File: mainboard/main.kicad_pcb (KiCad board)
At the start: 2 copper layers, 13 parts, among them U1 LevelShifter

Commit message: merge boards
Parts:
- removed Con_MainBoard2PowerBoard1: Conn_01x09_Female, Connector_PinSocket_2.54mm:PinSocket_1x11_P2.54mm_Vertical
- added Battery_Connector1: Conn_01x06, Connector_JST:JST_XH_B6B-XH-A_1x06_P2.50mm_Vertical, F.Cu at (147.3, 101.6)
- added C1: 1uF, Capacitor_THT:CP_Radial_D5.0mm_P2.50mm, F.Cu at (175.3, 101.6)
- added C2: 1uF, Capacitor_THT:CP_Radial_D5.0mm_P2.50mm, F.Cu at (157.5, 101.6)
- added CellVoltageOpAmp1: LM358, Package_DIP:DIP-8_W7.62mm_Socket, F.Cu at (172.7, 88.9)
- added Con_Stepdown_Board1: Conn_01x03, Connector_JST:JST_XH_B3B-XH-A_1x03_P2.50mm_Vertical, F.Cu at (188.0, 81.3)
- added CurrentDrawOpAmp1: LM358, Package_DIP:DIP-8_W7.62mm_Socket, F.Cu at (154.9, 88.9)
- added CurrentSensor1: ACS712Breakout, CustomFootprints:ACS712BreakoutBoardUpSideDown, F.Cu at (124.5, 88.9)
- added Diode1: D, Diode_THT:D_T-1_P5.08mm_Horizontal, F.Cu at (147.3, 73.7)
- added Q1: TIP120, Package_TO_SOT_THT:TO-220-3_Vertical, F.Cu at (115.6, 80.0)
- added RV1: R_POT_TRIM, Potentiometer_THT:Potentiometer_Bourns_3296W_Vertical, F.Cu at (127.0, 78.7)
- added R_Cell1_Vdiv_A1: 33K, Resistor_THT:R_Axial_DIN0207_L6.3mm_D2.5mm_P7.62mm_Horizontal, F.Cu at (170.2, 83.8)
- added R_Cell1_Vdiv_B1: 100K, Resistor_THT:R_Axial_DIN0207_L6.3mm_D2.5mm_P2.54mm_Vertical, F.Cu at (177.8, 83.8)
- added R_I_1: 10K, Resistor_THT:R_Axial_DIN0207_L6.3mm_D2.5mm_P5.08mm_Vertical, F.Cu at (142.2, 88.9)
- added R_I_2: 33K, Resistor_THT:R_Axial_DIN0207_L6.3mm_D2.5mm_P5.08mm_Vertical, F.Cu at (147.3, 91.4)
- added R_I_3: 33K, Resistor_THT:R_Axial_DIN0207_L6.3mm_D2.5mm_P2.54mm_Vertical, F.Cu at (144.8, 83.8)
- added R_I_4: 22K, Resistor_THT:R_Axial_DIN0207_L6.3mm_D2.5mm_P2.54mm_Vertical, F.Cu at (147.3, 91.4)
- added R_T1: 1K, Resistor_THT:R_Axial_DIN0207_L6.3mm_D2.5mm_P5.08mm_Vertical, F.Cu at (124.5, 100.3)
- added R_V_Cell2_1: 47K, Resistor_THT:R_Axial_DIN0207_L6.3mm_D2.5mm_P2.54mm_Vertical, F.Cu at (167.6, 91.4)
- added R_V_Cell2_2: 47K, Resistor_THT:R_Axial_DIN0207_L6.3mm_D2.5mm_P2.54mm_Vertical, F.Cu at (165.1, 101.6)
- added R_V_Cell2_3: 33K, Resistor_THT:R_Axial_DIN0207_L6.3mm_D2.5mm_P2.54mm_Vertical, F.Cu at (167.6, 91.4)
- added R_V_Cell2_4: 33K, Resistor_THT:R_Axial_DIN0207_L6.3mm_D2.5mm_P2.54mm_Vertical, F.Cu at (167.6, 99.1)
- added R_V_Cell3_1: 47K, Resistor_THT:R_Axial_DIN0207_L6.3mm_D2.5mm_P5.08mm_Vertical, F.Cu at (185.4, 94.0)
- added R_V_Cell3_2: 47K, Resistor_THT:R_Axial_DIN0207_L6.3mm_D2.5mm_P2.54mm_Vertical, F.Cu at (188.0, 96.5)
- added R_V_Cell3_3: 33K, Resistor_THT:R_Axial_DIN0207_L6.3mm_D2.5mm_P2.54mm_Vertical, F.Cu at (185.4, 94.0)
- added R_V_Cell3_4: 33K, Resistor_THT:R_Axial_DIN0207_L6.3mm_D2.5mm_P2.54mm_Vertical, F.Cu at (188.0, 91.4)
- added Switch_Connector1: Conn_01x04, Connector_JST:JST_XH_B2B-XH-A_1x02_P2.50mm_Vertical, F.Cu at (141.0, 78.7)
- moved AdOn_Connector1 18.2 mm to (116.8, 45.7)
- moved Con_Switch1 8.03 mm to (175.3, 76.2)
- moved U1 7.62 mm to (129.5, 40.6)
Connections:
- MicroController1 pad 17: PowerIN -> P_IN
- MicroController1 pad 18: PCheck -> P_Check
- MicroController1 pad 19: Net-(Con_MainBoard2PowerBoard1-Pad6) -> op1
- MicroController1 pad 20: Net-(Con_MainBoard2PowerBoard1-Pad5) -> op2
- MicroController1 pad 21: Net-(Con_MainBoard2PowerBoard1-Pad4) -> op3
- MicroController1 pad 23: Net-(Con_MainBoard2PowerBoard1-Pad3) -> op4
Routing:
- net GND: track 193.1 -> 348.3 mm, vias 0 -> 1
- net +BATT: track 111.8 -> 248.0 mm
- net +5V: track 65.4 -> 196.2 mm, vias 0 -> 1
- net op1: track 0.00 -> 44.6 mm
- net Net-(Diode1-Pad1): track 0.00 -> 43.6 mm
- net BATT_Cell_2_3: track 0.00 -> 40.2 mm
- net BATT_Cell_1_2: track 0.00 -> 38.2 mm
- net P_Check: track 0.00 -> 35.7 mm
- net op3: track 0.00 -> 34.3 mm
- net op2: track 0.00 -> 30.7 mm
- net Net-(Battery_Connector1-Pad5): track 0.00 -> 28.7 mm
- net +3V3: track 166.3 -> 194.8 mm
- net I2C_SDA: track 70.2 -> 95.6 mm
- net Net-(CurrentSensor1-Pad5): track 0.00 -> 23.7 mm
- net PCheck: track 22.0 -> 0.00 mm
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
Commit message: first prototype
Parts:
- removed C1: 1uF, Capacitor_THT:CP_Radial_D5.0mm_P2.50mm
- removed CellVoltageOpAmp1: LM358, Package_DIP:DIP-8_W7.62mm_Socket
- removed R_Cell1_Vdiv_A1: 33K, Resistor_THT:R_Axial_DIN0207_L6.3mm_D2.5mm_P7.62mm_Horizontal
- removed R_Cell1_Vdiv_B1: 100K, Resistor_THT:R_Axial_DIN0207_L6.3mm_D2.5mm_P2.54mm_Vertical
- removed R_V_Cell2_1, R_V_Cell2_2, R_V_Cell3_2: 47K, Resistor_THT:R_Axial_DIN0207_L6.3mm_D2.5mm_P2.54mm_Vertical
- removed R_V_Cell2_3, R_V_Cell2_4, R_V_Cell3_3, R_V_Cell3_4: 33K, Resistor_THT:R_Axial_DIN0207_L6.3mm_D2.5mm_P2.54mm_Vertical
- removed R_V_Cell3_1: 47K, Resistor_THT:R_Axial_DIN0207_L6.3mm_D2.5mm_P5.08mm_Vertical
- added Diode2: D, Diode_THT:D_T-1_P5.08mm_Horizontal, F.Cu at (167.6, 94.0)
- added Diode3: D, Diode_THT:D_T-1_P5.08mm_Horizontal, F.Cu at (180.3, 96.5)
- added R1: ?, Resistor_THT:R_Axial_DIN0207_L6.3mm_D2.5mm_P2.54mm_Vertical, F.Cu at (146.1, 73.7)
- added REF**: MountingHole_2.2mm_M2, MountingHole:MountingHole_2.2mm_M2, F.Cu at (111.8, 102.9)
- added REF**: MountingHole_2.2mm_M2, MountingHole:MountingHole_2.2mm_M2, F.Cu at (190.5, 102.9)
- added REF**: MountingHole_2.2mm_M2, MountingHole:MountingHole_2.2mm_M2, F.Cu at (190.5, 29.2)
- added REF**: MountingHole_2.2mm_M2, MountingHole:MountingHole_2.2mm_M2, F.Cu at (111.8, 29.2)
- added RV2: R_POT3Bat, Potentiometer_THT:Potentiometer_Bourns_3296W_Vertical, F.Cu at (167.6, 85.1)
- added RV3: R_POT2, Potentiometer_THT:Potentiometer_Bourns_3296W_Vertical, F.Cu at (174.0, 85.1)
- added RV4: R_POT1, Potentiometer_THT:Potentiometer_Bourns_3296W_Vertical, F.Cu at (180.3, 85.1)
- MicroController1: footprint CustomFootprints:Arduino_Pro_Mini_Socket_IZOKEE -> CustomFootprints:Arduino_Pro_Mini_Socket_IZOKEE_no_programming
- moved R_T1 25.4 mm to (123.2, 74.9)
- moved Diode1sw1 1.27 mm to (148.6, 73.7)
- renumbered Diode1 to Diode1sw1
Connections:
- Con_Switch1 pad 3: +3V3 -> GND
- Diode1sw1 pad 1: Net-(Diode1-Pad1) -> Net-(Diode1sw1-Pad1)
- RV1 pad 3: Net-(Diode1-Pad1) -> Net-(Diode1sw1-Pad1)
- R_T1 pad 1: Net-(Diode1-Pad1) -> Net-(Diode1sw1-Pad1)
- Switch_Connector1 pad 2: Net-(Diode1-Pad1) -> Net-(R1-Pad1)
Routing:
- net Net-(Diode1-Pad1): track 43.6 -> 0.00 mm
- net Net-(Diode1sw1-Pad1): track 0.00 -> 31.9 mm
- net BATT_Cell_2_3: track 40.2 -> 21.4 mm
- net GND: track 348.3 -> 329.5 mm, vias 1 -> 0
- net +5V: track 196.2 -> 179.2 mm, vias 1 -> 0
- net Net-(Q1-Pad1): track 21.9 -> 6.13 mm
- net +BATT: track 248.0 -> 262.5 mm
- net op3: track 34.3 -> 22.7 mm
- net Net-(R1-Pad1): track 0.00 -> 10.4 mm
- net Net-(CellVoltageOpAmp1-Pad3): track 9.72 -> 0.00 mm
- net +3V3: track 194.8 -> 186.0 mm
- net Net-(CellVoltageOpAmp1-Pad5): track 8.67 -> 0.00 mm
- net op2: track 30.7 -> 23.3 mm
- net Net-(Diode3-Pad1): track 0.00 -> 6.35 mm
- net op4: track 19.4 -> 25.1 mm
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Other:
- board text added: "CV & RS"

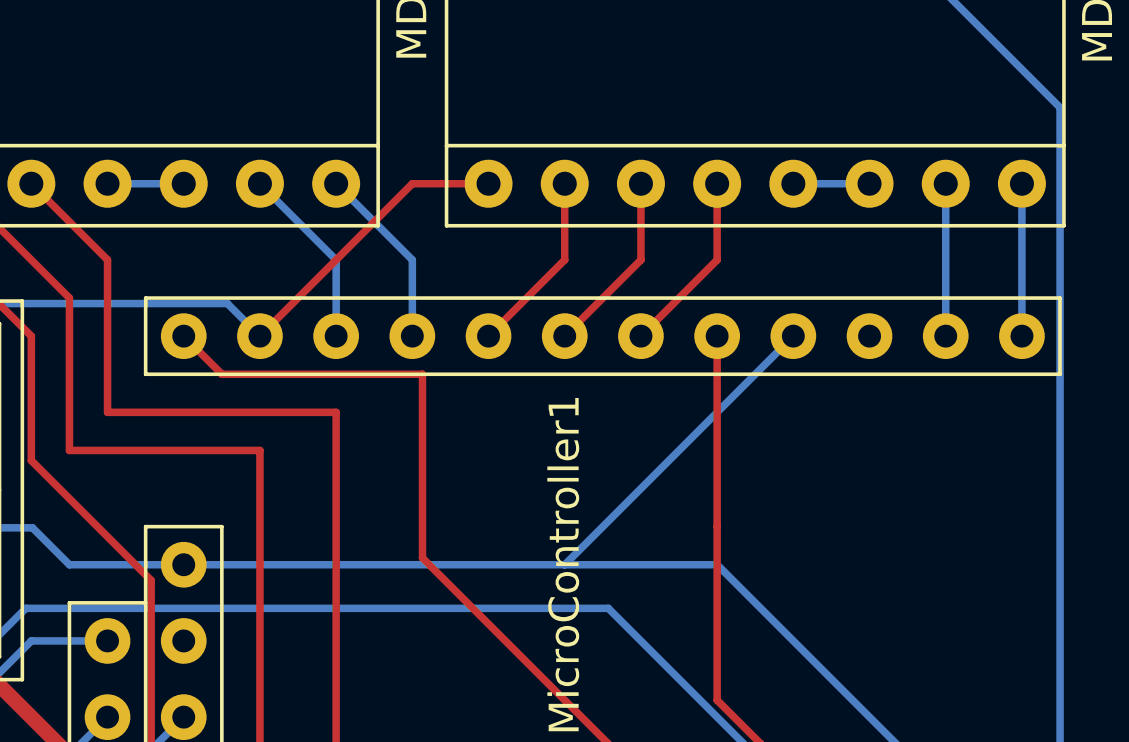
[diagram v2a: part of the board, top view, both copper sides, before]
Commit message: pwm pins
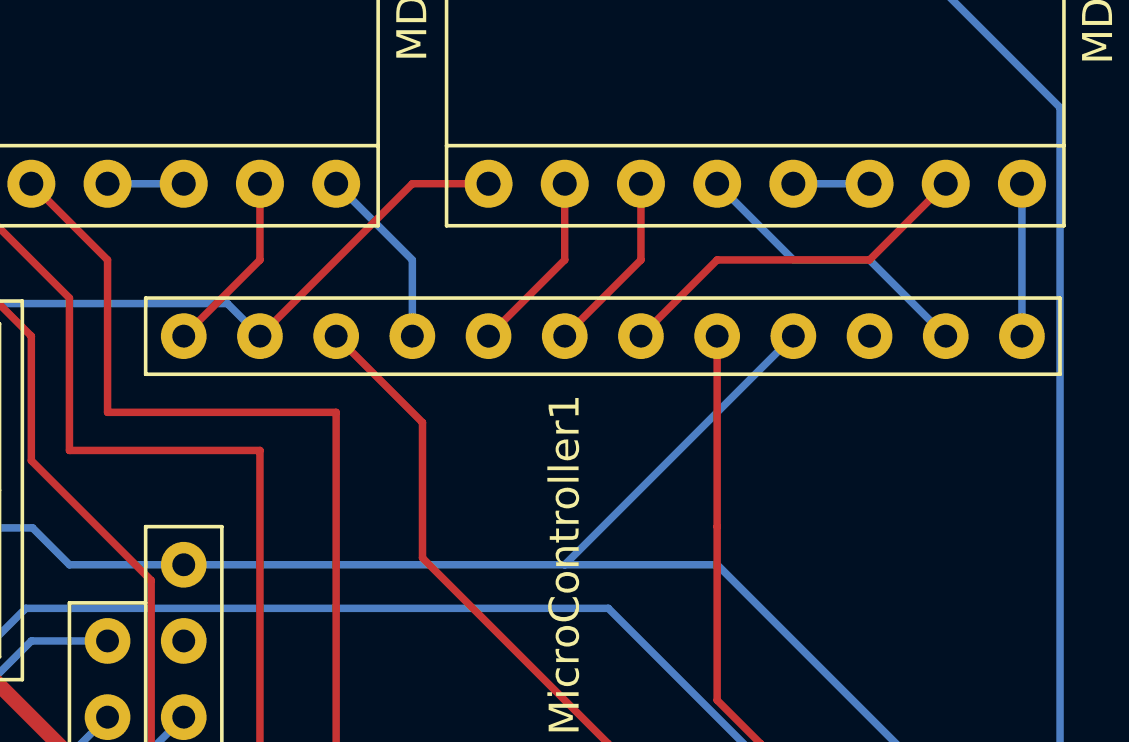
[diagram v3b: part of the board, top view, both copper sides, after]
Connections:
- MicroController1 pad 10: Step_L -> Sw2
- MicroController1 pad 12: Sw2 -> Step_L
- MicroController1 pad 2: Step_R -> MS3_R
- MicroController1 pad 6: MS3_R -> Step_R
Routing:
- net Step_R: track 5.08 -> 12.3 mm
- net Sw2: track 33.1 -> 27.1 mm
- net MS3_R: track 6.13 -> 9.72 mm
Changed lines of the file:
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@@
     (thickness 1.6)
     (drawings 22)
-    (tracks 337)
+    (tracks 339)
     (zones 0)
     (modules 36)
@@
   )
   (setup
-    (last_trace_width 0.5)
+    (last_trace_width 0.25)
     (user_trace_width 0.25)
     (user_trace_width 0.5)
@@
       (net 9 Dir_R))
     (pad 2 thru_hole circle (at -7.62 -10.16 270) (size 1.524 1.524) (drill 0.762) (layers *.Cu *.Mask)
-      (net 10 Step_R))
+      (net 35 MS3_R))
     (pad 3 thru_hole circle (at -7.62 -7.62 270) (size 1.524 1.524) (drill 0.762) (layers *.Cu *.Mask)
       (net 25 "Net-(MicroController1-Pad3)"))
@@
       (net 41 Sw1))
     (pad 6 thru_hole circle (at -7.62 0 270) (size 1.524 1.524) (drill 0.762) (layers *.Cu *.Mask)
-      (net 35 MS3_R))
+      (net 10 Step_R))
     (pad 7 thru_hole circle (at -7.62 2.54 270) (size 1.524 1.524) (drill 0.762) (layers *.Cu *.Mask)
       (net 36 MS2_R))
@@
       (net 6 Dir_L))
     (pad 10 thru_hole circle (at -7.62 10.16 270) (size 1.524 1.524) (drill 0.762) (layers *.Cu *.Mask)
-      (net 7 Step_L))
+      (net 42 Sw2))
     (pad 11 thru_hole circle (at -7.62 12.7 270) (size 1.524 1.524) (drill 0.762) (layers *.Cu *.Mask)
       (net 8 Enable_Steppers))
     (pad 12 thru_hole circle (at -7.62 15.24 270) (size 1.524 1.524) (drill 0.762) (layers *.Cu *.Mask)
-      (net 42 Sw2))
+      (net 7 Step_L))
     (pad 13 thru_hole circle (at 7.62 15.24 270) (size 1.524 1.524) (drill 0.762) (layers *.Cu *.Mask)
       (net 34 MS1_L))
@@
   (segment (start 167.64 53.34) (end 167.64 50.8) (width 0.25) (layer B.Cu) (net 6))
   (segment (start 167.64 50.8) (end 165.1 48.26) (width 0.25) (layer B.Cu) (net 6))
-  (segment (start 165.1 50.8) (end 162.56 48.26) (width 0.25) (layer B.Cu) (net 7))
-  (segment (start 165.1 53.34) (end 165.1 50.8) (width 0.25) (layer B.Cu) (net 7))
+  (segment (start 162.56 50.8) (end 160.02 53.34) (width 0.25) (layer F.Cu) (net 7))
+  (segment (start 162.56 48.26) (end 162.56 50.8) (width 0.25) (layer F.Cu) (net 7))
   (segment (start 151.312999 52.252999) (end 148.119999 49.059999) (width 0.25) (layer B.Cu) (net 8))
   (segment (start 148.119999 49.059999) (end 147.32 48.26) (width 0.25) (layer B.Cu) (net 8))
@@
   (segment (start 162.56 53.34) (end 167.64 48.26) (width 0.25) (layer F.Cu) (net 8))
   (segment (start 187.96 53.34) (end 187.96 48.26) (width 0.25) (layer B.Cu) (net 9))
-  (segment (start 185.42 48.26) (end 185.42 53.34) (width 0.25) (layer B.Cu) (net 10))
+  (segment (start 175.26 53.34) (end 177.8 50.8) (width 0.25) (layer F.Cu) (net 10))
+  (segment (start 182.88 50.8) (end 185.42 48.26) (width 0.25) (layer F.Cu) (net 10))
+  (segment (start 177.8 50.8) (end 182.88 50.8) (width 0.25) (layer F.Cu) (net 10))
   (segment (start 161.195001 36.924999) (end 161.760001 36.359999) (width 0.25) (layer B.Cu) (net 11))
   (segment (start 161.760001 36.359999) (end 162.56 35.56) (width 0.25) (layer B.Cu) (net 11))
@@
   (segment (start 154.94 57.488762) (end 158.932999 61.481761) (width 0.25) (layer F.Cu) (net 34))
   (segment (start 154.94 53.34) (end 154.94 57.488762) (width 0.25) (layer F.Cu) (net 34))
-  (segment (start 177.8 50.8) (end 175.26 53.34) (width 0.25) (layer F.Cu) (net 35))
-  (segment (start 177.8 48.26) (end 177.8 50.8) (width 0.25) (layer F.Cu) (net 35))
+  (segment (start 185.42 53.34) (end 182.88 50.8) (width 0.25) (layer B.Cu) (net 35))
+  (segment (start 180.34 50.8) (end 177.8 48.26) (width 0.25) (layer B.Cu) (net 35))
+  (segment (start 182.88 50.8) (end 180.34 50.8) (width 0.25) (layer B.Cu) (net 35))
   (segment (start 175.26 50.8) (end 172.72 53.34) (width 0.25) (layer F.Cu) (net 36))
   (segment (start 175.26 48.26) (end 175.26 50.8) (width 0.25) (layer F.Cu) (net 36))
@@
   (segment (start 175.26 73.66) (end 175.26 76.2) (width 0.25) (layer F.Cu) (net 42))
   (segment (start 174.172999 72.572999) (end 175.26 73.66) (width 0.25) (layer F.Cu) (net 42))
-  (segment (start 161.29 54.61) (end 167.978762 54.61) (width 0.25) (layer F.Cu) (net 42))
-  (segment (start 160.02 53.34) (end 161.29 54.61) (width 0.25) (layer F.Cu) (net 42))
-  (segment (start 167.978762 54.61) (end 167.978762 60.733522) (width 0.25) (layer F.Cu) (net 42))
   (segment (start 174.172999 66.927759) (end 174.172999 72.572999) (width 0.25) (layer F.Cu) (net 42))
   (segment (start 167.978762 60.733522) (end 174.172999 66.927759) (width 0.25) (layer F.Cu) (net 42))
+  (segment (start 167.978762 56.218762) (end 167.978762 60.733522) (width 0.25) (layer F.Cu) (net 42))
+  (segment (start 165.1 53.34) (end 167.978762 56.218762) (width 0.25) (layer F.Cu) (net 42))
   (segment (start 144.82 101.475) (end 148.360001 97.934999) (width 0.25) (layer F.Cu) (net 43))
   (segment (start 144.82 101.6) (end 144.82 101.475) (width 0.25) (layer F.Cu) (net 43))

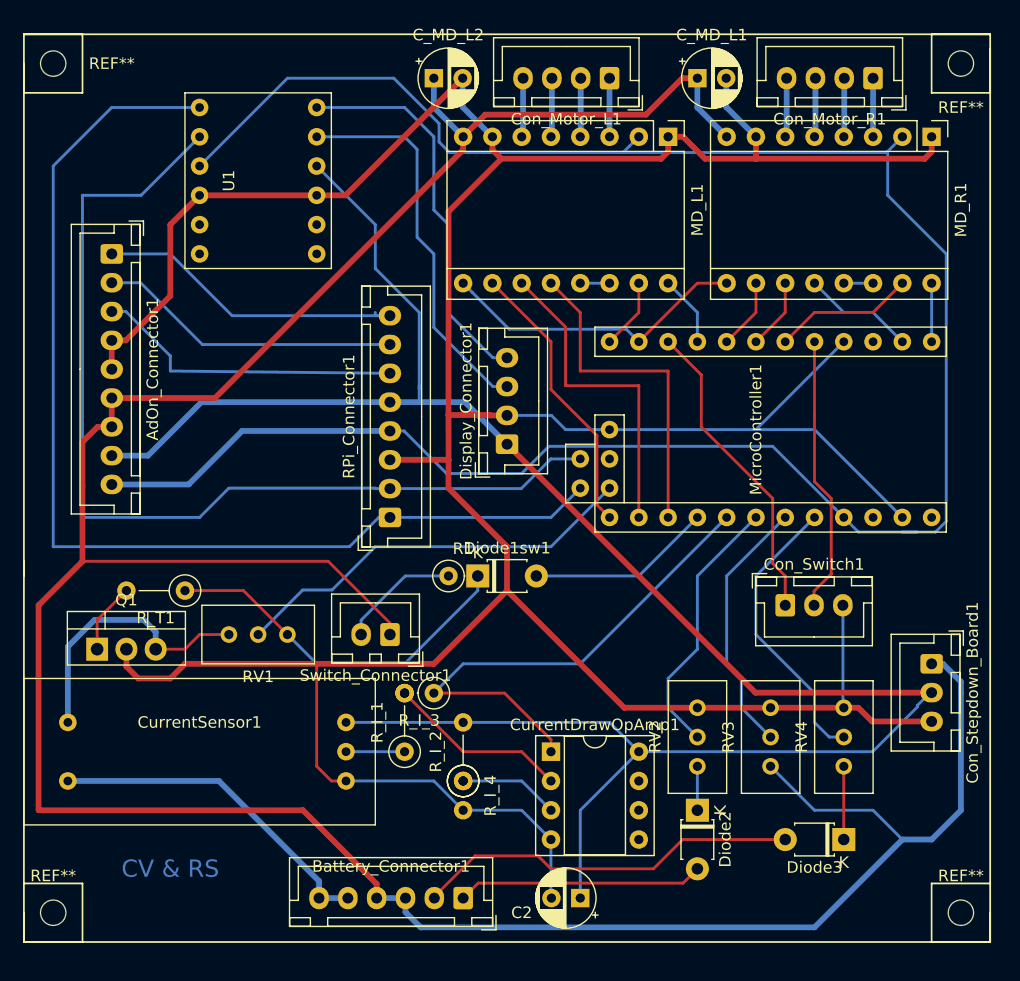
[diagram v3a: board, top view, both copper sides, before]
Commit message: larger capacitor footprints
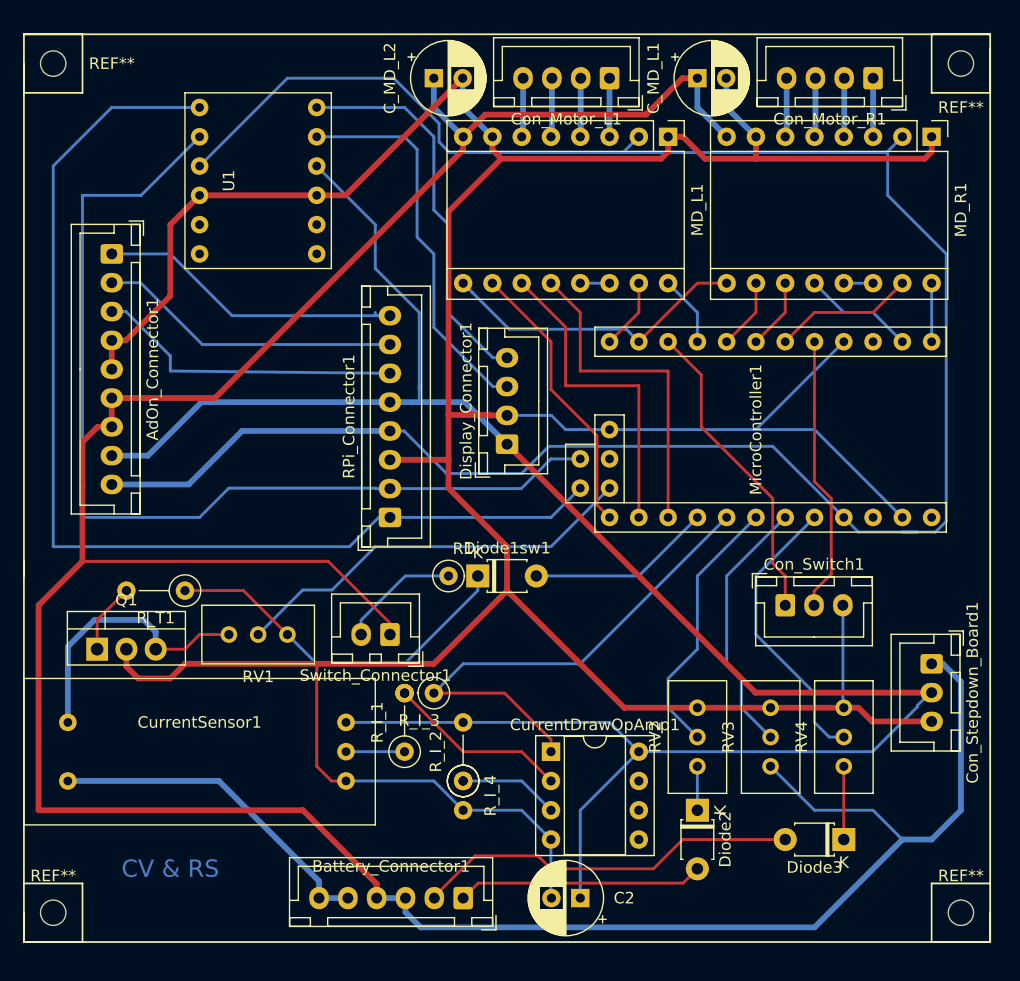
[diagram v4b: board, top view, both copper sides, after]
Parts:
- C2, C_MD_L1, C_MD_L2: footprint Capacitor_THT:CP_Radial_D5.0mm_P2.50mm -> Capacitor_THT:CP_Radial_D6.3mm_P2.50mm

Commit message: Mainboard changes
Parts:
- C2, C_MD_L1, C_MD_L2: footprint Capacitor_THT:CP_Radial_D6.3mm_P2.50mm -> Capacitor_THT:CP_Radial_D5.0mm_P2.50mm
- moved Battery_Connector1 65.6 mm to (130.8, 38.1), turned to 270 degrees
- moved AdOn_Connector1 48.3 mm to (115.6, 94.0), turned to 0 degrees
- moved Q1 43.0 mm to (139.7, 44.5), turned to 270 degrees
- moved RPi_Connector1 26.2 mm to (115.6, 62.2), turned to 270 degrees
- moved R_T1 26.1 mm to (142.2, 57.1)
- moved RV1 19.1 mm to (138.4, 63.5), turned to 90 degrees
- moved CurrentSensor1 18.2 mm to (128.3, 71.1), turned to 270 degrees
- moved U1 12.8 mm to (116.8, 41.9)
- moved Diode2 10.8 mm to (175.9, 101.0), turned to 0 degrees
- moved R_I_1 7.18 mm to (137.2, 83.8), turned to 0 degrees
- turned Diode3 to 0 degrees
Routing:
- net BATT_Cell_2_3: track 21.4 -> 148.3 mm
- net BATT_Cell_1_2: track 33.5 -> 135.0 mm
- net +BATT: track 262.5 -> 202.8 mm
- net +3V3: track 186.0 -> 226.7 mm
- net GND: track 329.5 -> 369.0 mm
- net I2C_SDA: track 95.6 -> 74.2 mm
- net Net-(Battery_Connector1-Pad5): track 29.6 -> 13.7 mm
- net RPI3: track 27.9 -> 14.2 mm
- net +5V: track 179.2 -> 191.7 mm
- net P_Check: track 35.7 -> 23.7 mm
- net Net-(Diode2-Pad1): track 3.81 -> 14.9 mm
- net Net-(Display_Connector1-Pad4): track 33.7 -> 44.7 mm
- net Net-(Display_Connector1-Pad3): track 33.7 -> 42.2 mm
- net Net-(Q1-Pad1): track 6.13 -> 14.6 mm
- net Net-(Diode1sw1-Pad1): track 31.9 -> 23.5 mm
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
